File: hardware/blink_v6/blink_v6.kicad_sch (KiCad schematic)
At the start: 241 parts, among them J1 RJ45, J12 Conn_01x06, J2 Conn_01x06_Pin, J3 Conn_01x05_Pin, J4 Conn_01x04_Pin, J5 Conn_01x06_Pin, J6 Conn_01x04_Pin, J7 Conn_01x04_Pin, J8 Conn_01x02, J9 Conn_02x10_Odd_Even, Q1 2N7002, Q10 2N7002, Q2 2N7002, Q3 2N7002, Q4 2N7002, Q5 2N7002, Q6 2N7002, Q7 2N7002, Q8 2N7002, Q9 2N7002, U1 ADA4807-1, U10 STM32F405RGTx, U11 AMS1117-3.3, U12 BA50DD0WHFP-TR, U13 M24C02-RMN, U2 SN74LVC1G14DBV, U3 SN74LVC1G14DBV, U4 ADA4807-1, U5 ADA4807-1, U6 TLV3603DCKR, U7 SN74LVC1G14DBV, U8 TLV3603DCKR, U9 L78L05_SOT89, X2 GTXO-14V (2.048MHz), Y1 AOCJY4A-10.000MHZ-SW, Y2 16MHz

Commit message: star clean up of blink board
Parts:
- removed ANT3, ANT4, ANT5, ANT6: U.FL-R-SMT-1, blinky_footprints:U.FL-R-SMT-1, symbol blinky:U.FL-R-SMT-1
- removed C1, C10, C17, C18, C2, C25, C26, C33, C45, C46, C48, C49: 100nF, Capacitor_SMD:C_0402_1005Metric, symbol Device:C_Small
- removed C12, C14, C19, C23, C5, C7: 150pF, Capacitor_SMD:C_0603_1608Metric, symbol Device:C_Small
- removed C13, C20, C8: 330pF, Capacitor_SMD:C_0603_1608Metric, symbol Device:C_Small
- removed C15, C22, C6: 220pF, Capacitor_SMD:C_0603_1608Metric, symbol Device:C_Small
- removed C16, C21, C3: 1nF, Capacitor_SMD:C_0603_1608Metric, symbol Device:C_Small
- removed C24: 100nF, Capacitor_SMD:C_0603_1608Metric, symbol Device:C_Small
- removed C34: 10uF, Capacitor_Tantalum_SMD:CP_EIA-3216-18_Kemet-A, symbol Device:C_Polarized
- removed C42, C44: 33uF, Capacitor_Tantalum_SMD:CP_EIA-3528-21_Kemet-B, symbol Device:C_Polarized
- removed J1: RJ45, Connector_RJ:RJ45_Amphenol_RJHSE5380, symbol Connector:RJ45
- removed J2: Conn_01x06_Pin, Connector_PinHeader_2.54mm:PinHeader_1x06_P2.54mm_Vertical, symbol Connector:Conn_01x06_Pin
- removed J3: Conn_01x05_Pin, Connector_PinHeader_2.54mm:PinHeader_1x05_P2.54mm_Vertical, symbol Connector:Conn_01x05_Pin
- removed JP1: SolderJumper_2_Bridged, Jumper:SolderJumper-2_P1.3mm_Bridged_RoundedPad1.0x1.5mm, symbol Jumper:SolderJumper_2_Bridged
- removed L1, L2, L3, L4, L5, L6: 1uF, Inductor_SMD:L_0805_2012Metric, symbol Device:L_Small
- removed R1, R15, R16: 100R, Resistor_SMD:R_0603_1608Metric, symbol Device:R_Small_US
- removed R10, R2, R6: 510R, Resistor_SMD:R_0603_1608Metric, symbol Device:R_Small_US
- removed R11, R3, R7: 49R9, Resistor_SMD:R_0603_1608Metric, symbol Device:R_Small_US
- removed R12, R13: 1K5, Resistor_SMD:R_0805_2012Metric, symbol Device:R_Small_US
- removed R14: 330R, Resistor_SMD:R_0805_2012Metric, symbol Device:R_Small_US
- removed R17: 20R, Resistor_SMD:R_0805_2012Metric, symbol Device:R_Small_US
- removed R18, R21: 130K, Resistor_SMD:R_0603_1608Metric, symbol Device:R_Small_US
- removed R19, R20, R22, R24, R60, R61: 1K0, Resistor_SMD:R_0603_1608Metric, symbol Device:R_Small_US
- removed R23: 22K, Resistor_SMD:R_0805_2012Metric, symbol Device:R_Small_US
- removed R25: 270R, Resistor_SMD:R_0603_1608Metric, symbol Device:R_Small_US
- removed R26: 22R0, Resistor_SMD:R_0603_1608Metric, symbol Device:R_Small_US
- removed R8: 270R, Resistor_SMD:R_0805_2012Metric, symbol Device:R_Small_US
- removed R9: 2R, Resistor_SMD:R_0805_2012Metric, symbol Device:R_Small_US
- removed RV1: 20K, Potentiometer_SMD:Potentiometer_Bourns_3314G_Vertical, symbol Device:R_Potentiometer_US
- removed TP10, TP11, TP15, TP18, TP19, TP5, TP6, TP7, TP8, TP9: ~, TestPoint:TestPoint_THTPad_D1.5mm_Drill0.7mm, symbol Connector:TestPoint
- removed U1, U4, U5: ADA4807-1, Package_TO_SOT_SMD:SOT-23-6, symbol Amplifier_Operational:ADA4807-1
- removed U12: BA50DD0WHFP-TR, blinky_footprints:DPAK172P1054X200-6N, symbol blinky:BA50DD0WHFP-TR
- removed U6: TLV3603DCKR, blinky_footprints:SC70_DCK_TEX, symbol blinky:TLV3603DCKR
- removed U7: SN74LVC1G14DBV, Package_TO_SOT_SMD:SOT-23-5, symbol 74xGxx:SN74LVC1G14DBV
- removed U8: TLV3603DCKR, SC70_DCK_TEX, symbol blinky:TLV3603DCKR
- removed U9: L78L05_SOT89, Package_TO_SOT_SMD:SOT-89-3, symbol Regulator_Linear:L78L05_SOT89
- removed Y1: AOCJY4A-10.000MHZ-SW, blinky_footprints:XTAL_AOCJY4A-10.000MHZ-SW, symbol blinky:AOCJY4A-10.000MHZ-SW
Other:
- note removed: "12 MHz 5th Order Butterworth Lowpass"
- note removed: "3.1 MHz RC Highpass filter"

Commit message: moved parts from audio test board into blink board
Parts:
- added C? (x3): 0.1uF, Capacitor_SMD:C_0805_2012Metric, symbol Device:C_Small
- added C? (x3): 10uF, Capacitor_SMD:C_0805_2012Metric, symbol Device:C_Small
- added C?: 10uF, Capacitor_Tantalum_SMD:CP_EIA-3216-18_Kemet-A, symbol Device:C_Polarized_Small_US
- added J?: Conn_01x04_Pin, Connector_PinHeader_2.54mm:PinHeader_1x04_P2.54mm_Vertical_SMD_Pin1Left, symbol Connector:Conn_01x04_Pin
- added J? (x2): KH-BNC50-3511, blinky_footprints:BNC_Amphenol_B6252HB-NPP3G-50_Horizontal-CJ, symbol Connector:Conn_Coaxial
- added J? (x2): PJ-320D, blinky_footprints:Jack_3.5mm_PJ320D_Horizontal-CJ, symbol Connector_Audio:AudioJack4
- added R?: 22K, Resistor_SMD:R_0805_2012Metric, symbol Device:R_Small_US
- added R? (x4): 47k, Resistor_SMD:R_0805_2012Metric, symbol Device:R_Small_US
- added R? (x3): 560R, Resistor_SMD:R_0805_2012Metric, symbol Device:R_Small_US
- added R?: 100R, Resistor_SMD:R_0805_2012Metric, symbol Device:R_Small_US
- added R?: 1K, Resistor_SMD:R_0805_2012Metric, symbol Device:R_Small_US
- added R?: 10K, Resistor_SMD:R_0805_2012Metric, symbol Device:R_Small_US
- added U? (x3): AD8397, Package_SO:SOIC-8_3.9x4.9mm_P1.27mm, symbol Amplifier_Operational:LM358
- renumbered ANT2 to ANT1, ANT1 to ANT2, C39 to C1, C27 to C10, C29 to C11, C32 to C12, C28 to C14, C36 to C15, C35 to C16, C31 to C18, C40 to C19, C43 to C2, C47 to C20, C38 to C21, C30 to C22, C11 to C23, C9 to C24, C4 to C25, C41 to C3, C37 to C4, D42 to D10, D17 to D11, D18 to D12, D15 to D13, D16 to D14, D12 to D15, D10 to D16, D6 to D17, D43 to D18, D44 to D19, D45 to D20, D19 to D21, D20 to D22, D21 to D23, D22 to D24, D13 to D25, D37 to D26, D38 to D27, D39 to D28, D28 to D29, D34 to D30, D25 to D32, D14 to D33, D46 to D34, D47 to D35, D48 to D36, D29 to D37, D35 to D38, D32 to D39, D8 to D4, D26 to D40, D23 to D41, D11 to D42, D7 to D43, D49 to D44, D50 to D45, D51 to D46, D30 to D47, D36 to D48, D33 to D49, D4 to D5, D27 to D50, D24 to D51, D5 to D6, D9 to D7, D40 to D8, D41 to D9, H5 to H2, H2 to H3, H3 to H4, H4 to H5, J8 to J1, J9 to J14, J7 to J5, J5 to J7, J12 to J8, J4 to J9, Q9 to Q1, Q4 to Q10, Q10 to Q2, Q5 to Q3, Q1 to Q4, Q2 to Q5, Q3 to Q8, Q8 to Q9, R58 to R12, R28 to R14, R59 to R15, R54 to R17, R32 to R18, R30 to R19, R62 to R20, R29 to R21, R31 to R22, R5 to R23, R4 to R24, R41 to R25, R33 to R26, R42 to R27, R63 to R28, R64 to R29, R34 to R30, R35 to R31, R43 to R32, R36 to R33, R44 to R34, R50 to R35, R49 to R36, R55 to R37, R56 to R38, R57 to R39, R52 to R40, R53 to R41, R51 to R42, R45 to R43, R37 to R44, R46 to R45, R38 to R46, R39 to R48, R48 to R49, R40 to R50, R27 to R9, TP17 to TP1, TP16 to TP2, TP12 to TP3, TP13 to TP4, TP14 to TP5, TP1 to TP6, TP4 to TP7, TP2 to TP8, TP3 to TP9, U11 to U1, U13 to U3, U10 to U4, U2 to U5, U3 to U6, X2 to X1, Y2 to Y1
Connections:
- net +3.3V: now also C?.1, C?.2, R?.2, R?.2, U?.8 (V+)
- net GND: now also C?.1, C?.1, C?.1, C?.2, J?.2 (Ext), J?.2 (Ext), J?.R2, J?.R2, R?.1, R?.1, R?.2, U?.4 (V-)
- new net: C?.2, J?.4 (Pin_4), R?.1, R?.2, R?.2
- new net: J?.1 (Pin_1), R?.1, R?.2, U?.2 (-)
- new net: J?.2 (Pin_2), R?.1, R?.2, U?.1
- new net: J?.3 (Pin_3), R?.1, R?.2, U?.5 (+)
- new net: C?.1, R?.1
- new net: C?.1, J?.1 (In), R?.1
- new net: J?.1 (In), R?.1
- new net: R?.2, U?.6 (-), U?.7
- new net: C?.1, R?.2
- new net: C?.2, R?.1, R?.2, U?.3 (+)
- new net: C?.2, R?.1
- new net Left: C?.2, J?.T, J?.T
- new net Mic: C?.2, J?.S, J?.S
- new net Right: J?.R1, J?.R1
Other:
- note added: "To Headset"
- note added: "To iPhone"
- moved on the sheet: ANT1, ANT2, C1, C10, C11, C12, C14, C15, C16, C18, C19, C2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

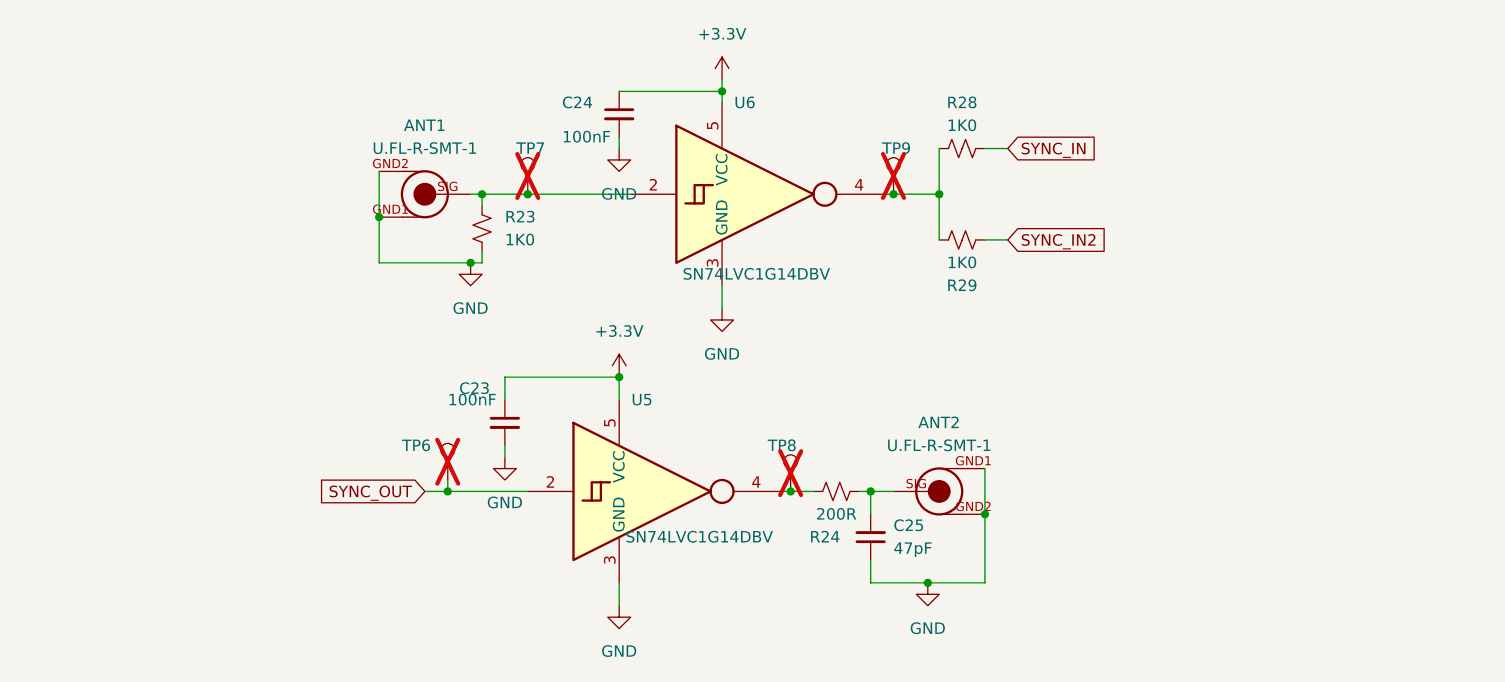
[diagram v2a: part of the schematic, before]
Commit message: updating board shape
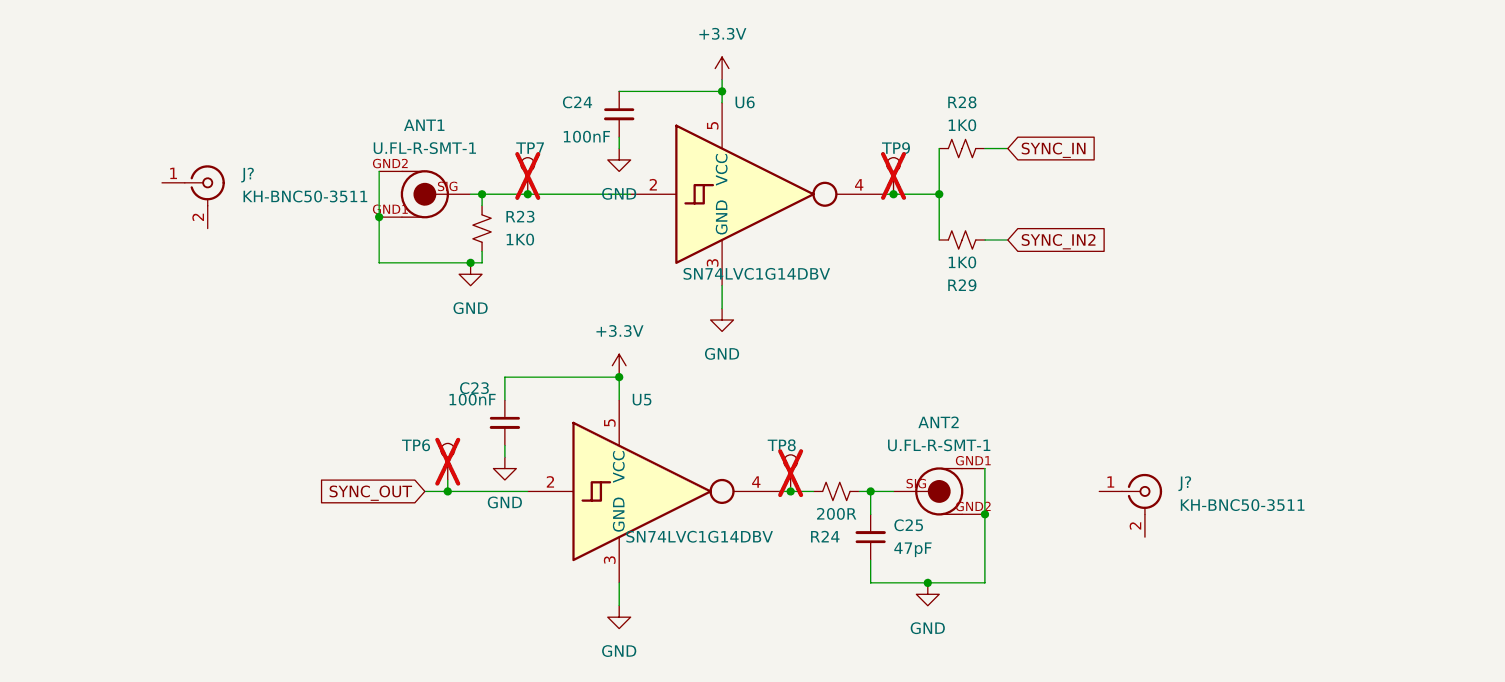
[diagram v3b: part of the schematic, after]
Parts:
- added J? (x2): KH-BNC50-3511, blinky_footprints:BNC_Amphenol_B6252HB-NPP3G-50_Horizontal-CJ, symbol Connector:Conn_Coaxial
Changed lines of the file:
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@@
     )
   )
+  (symbol (lib_id "Connector:Conn_Coaxial") (at 415.29 351.79 0) (unit 1)
+    (in_bom yes) (on_board yes) (dnp no) (fields_autoplaced)
+    (property "Reference" "J?" (at 419.1 350.8132 0)
+      (effects (font (size 1.27 1.27)) (justify left))
+    )
+    (property "Value" "KH-BNC50-3511" (at 419.1 353.3532 0)
+      (effects (font (size 1.27 1.27)) (justify left))
+    )
+    (property "Footprint" "blinky_footprints:BNC_Amphenol_B6252HB-NPP3G-50_Horizontal-CJ" (at 415.29 351.79 0)
+      (effects (font (size 1.27 1.27)) hide)
+    )
+    (property "Datasheet" "KH-BNC50-3511.pdf" (at 415.29 351.79 0)
+      (effects (font (size 1.27 1.27)) hide)
+    )
+    (property "JLCPCB Part #" "C2837587" (at 415.29 351.79 0)
+      (effects (font (size 1.27 1.27)) hide)
+    )
+    (property "MPN" "KH-BNC50-3511" (at 415.29 351.79 0)
+      (effects (font (size 1.27 1.27)) hide)
+    )
+    (property "JLCPCB Rotation Offset" "180" (at 415.29 351.79 0)
+      (effects (font (size 1.27 1.27)) hide)
+    )
+    (property "Sim.Enable" "0" (at 415.29 351.79 0)
+      (effects (font (size 1.27 1.27)) hide)
+    )
+    (pin "1")
+    (pin "2")
+    (instances
+      (project "audio_amp_r1"
+        (path "/65a2a7ad-257a-48a0-a706-3da4b4be7c88"
+          (reference "J?") (unit 1)
+        )
+      )
+      (project "blink_v6"
+        (path "/bd4d3b9a-07c1-4a53-9c94-2893f3e869d4"
+          (reference "J12") (unit 1)
+        )
+      )
+    )
+  )
   (symbol (lib_id "Device:R_US") (at 260.35 129.54 270) (unit 1)
     (in_bom yes) (on_board yes) (dnp no)
@@
         )
       )
+    )
+  )
+  (symbol (lib_id "Connector:Conn_Coaxial") (at 311.15 317.5 0) (unit 1)
+    (in_bom yes) (on_board yes) (dnp no) (fields_autoplaced)
+    (property "Reference" "J?" (at 314.96 316.5232 0)
+      (effects (font (size 1.27 1.27)) (justify left))
+    )
+    (property "Value" "KH-BNC50-3511" (at 314.96 319.0632 0)
+      (effects (font (size 1.27 1.27)) (justify left))
+    )
+    (property "Footprint" "blinky_footprints:BNC_Amphenol_B6252HB-NPP3G-50_Horizontal-CJ" (at 311.15 317.5 0)
+      (effects (font (size 1.27 1.27)) hide)
+    )
+    (property "Datasheet" "KH-BNC50-3511.pdf" (at 311.15 317.5 0)
+      (effects (font (size 1.27 1.27)) hide)
+    )
+    (property "JLCPCB Part #" "C2837587" (at 311.15 317.5 0)
+      (effects (font (size 1.27 1.27)) hide)
+    )
+    (property "MPN" "KH-BNC50-3511" (at 311.15 317.5 0)
+      (effects (font (size 1.27 1.27)) hide)
+    )
+    (property "JLCPCB Rotation Offset" "180" (at 311.15 317.5 0)
+      (effects (font (size 1.27 1.27)) hide)
+    )
+    (property "Sim.Enable" "0" (at 311.15 317.5 0)
+      (effects (font (size 1.27 1.27)) hide)
+    )
+    (pin "1")
+    (pin "2")
+    (instances
+      (project "audio_amp_r1"
+        (path "/65a2a7ad-257a-48a0-a706-3da4b4be7c88"
+          (reference "J?") (unit 1)
+        )
+      )
+      (project "blink_v6"
+        (path "/bd4d3b9a-07c1-4a53-9c94-2893f3e869d4"
+          (reference "J4") (unit 1)
+        )
+      )

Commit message: start re-layout of board
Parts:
- removed ANT1, ANT2: U.FL-R-SMT-1, blinky_footprints:U.FL-R-SMT-1, symbol blinky:U.FL-R-SMT-1
- removed D1, D16, D17, D4, D42, D43, D5, D6, D7: LED-RED, LED_SMD:LED_0603_1608Metric, symbol Device:LED
- removed D10, D11, D12, D13, D14, D15, D18, D19, D2, D20, D21, D22, D23, D24, D25, D26, D27, D28, D29, D30, D31, D32, D33, D34, D35, D36, D37, D38, D39, D40, D41, D44, D45, D46, D47, D48, D49, D50, D51, D8, D9: LED-G, LED_SMD:LED_0603_1608Metric, symbol Device:LED
- removed D3: LED-Y, LED_SMD:LED_0603_1608Metric, symbol Device:LED
- removed H2: M2, MountingHole:MountingHole_2.2mm_M2, symbol Mechanical:MountingHole
- removed J14: Conn_02x10_Odd_Even, Connector_PinHeader_2.54mm:PinHeader_2x10_P2.54mm_Vertical, symbol Connector_Generic:Conn_02x10_Odd_Even
- removed Q1, Q10, Q2, Q3, Q4, Q5, Q6, Q7, Q8, Q9: 2N7002, Package_TO_SOT_SMD:SOT-23, symbol Transistor_FET:2N7002
- removed R19, R21, R22, R27, R30, R33, R34, R45, R46, R49, R50: 100R, Resistor_SMD:R_0603_1608Metric, symbol Device:R_US
- removed R25, R26, R31, R32, R43, R44, R47, R48: 4K7, Resistor_SMD:R_0603_1608Metric, symbol Device:R_US
- removed R35, R36, R37, R38, R39, R40, R41, R42: 82R, Resistor_SMD:R_0603_1608Metric, symbol Device:R_US
- removed TP1, TP2, TP3, TP4, TP5, TP6, TP7, TP8, TP9: ~, TestPoint:TestPoint_THTPad_D1.5mm_Drill0.7mm, symbol Connector:TestPoint
- added J14: Conn_02x16_Odd_Even, Connector_PinHeader_2.54mm:PinHeader_2x16_P2.54mm_Vertical, symbol Connector_Generic:Conn_02x16_Odd_Even
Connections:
- net +3.3V: now also J14.1 (Pin_1); no longer C?.1, C?.2, R?.2, R?.2, U?.8 (V+)
- net +3.3VA: now also C?.1, C?.2, R?.2, R?.2, U?.8 (V+)
- net +6V: now also J14.2 (Pin_2)
- net AUX_SYNC_MON: now also J7.2 (Pin_2)
- net COL1: now also J14.7 (Pin_7)
- net COL2: now also J14.10 (Pin_10)
- net COL3: now also J14.6 (Pin_6)
- net COL4: now also J14.8 (Pin_8)
- net COL5: now also J14.5 (Pin_5)
- net GND: now also J?.2 (Ext), J?.2 (Ext), J14.3 (Pin_3), J14.4 (Pin_4)
- net LEDA: now also J14.27 (Pin_27)
- net LEDB: now also J14.19 (Pin_19)
- net LEDC: now also J14.20 (Pin_20)
- net LEDD: now also J14.17 (Pin_17)
- net LEDE: now also J14.18 (Pin_18)
- net LEDF: now also J14.11 (Pin_11)
- net LEDG: now also J14.12 (Pin_12)
- net LEDH: now also J14.9 (Pin_9)
- net LEDM1: now also J14.23 (Pin_23)
- net LEDM2: now also J14.26 (Pin_26)
- net LEDM3: now also J14.25 (Pin_25)
- net ROW1: now also J14.15 (Pin_15)
- net ROW2: now also J14.16 (Pin_16)
- net ROW3: now also J14.13 (Pin_13)
- net ROW4: now also J14.14 (Pin_14)
- net ROW5: now also J14.28 (Pin_28)
- net ROW6: now also J14.22 (Pin_22)
- net ROW7: now also J14.21 (Pin_21)
- net ROW8: now also J14.24 (Pin_24)
- net SYNC_OUT: no longer J7.2 (Pin_2)
- net at C25.2, R24.2: now also J?.1 (In)
- net at R23.1, U6.2: now also J?.1 (In)
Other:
- moved on the sheet: H4, H5, J9, J?
